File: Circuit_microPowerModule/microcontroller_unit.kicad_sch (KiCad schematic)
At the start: 1 part, among them U6 RP2040

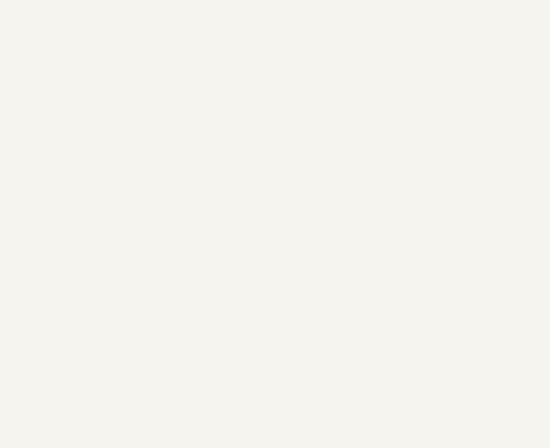
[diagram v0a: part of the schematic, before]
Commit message: added MP2315S lib, updated circuit
updated block diagram by-sa
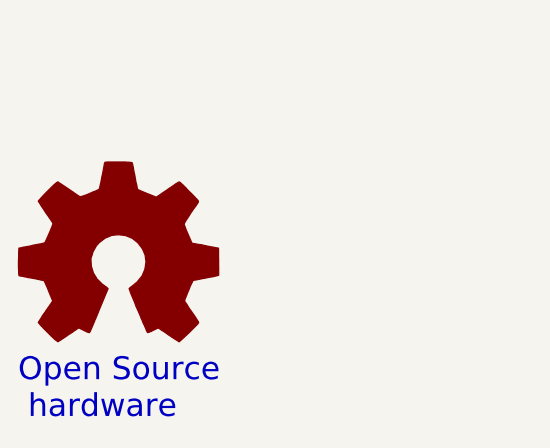
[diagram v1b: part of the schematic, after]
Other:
- note added: "Open Source hardware"

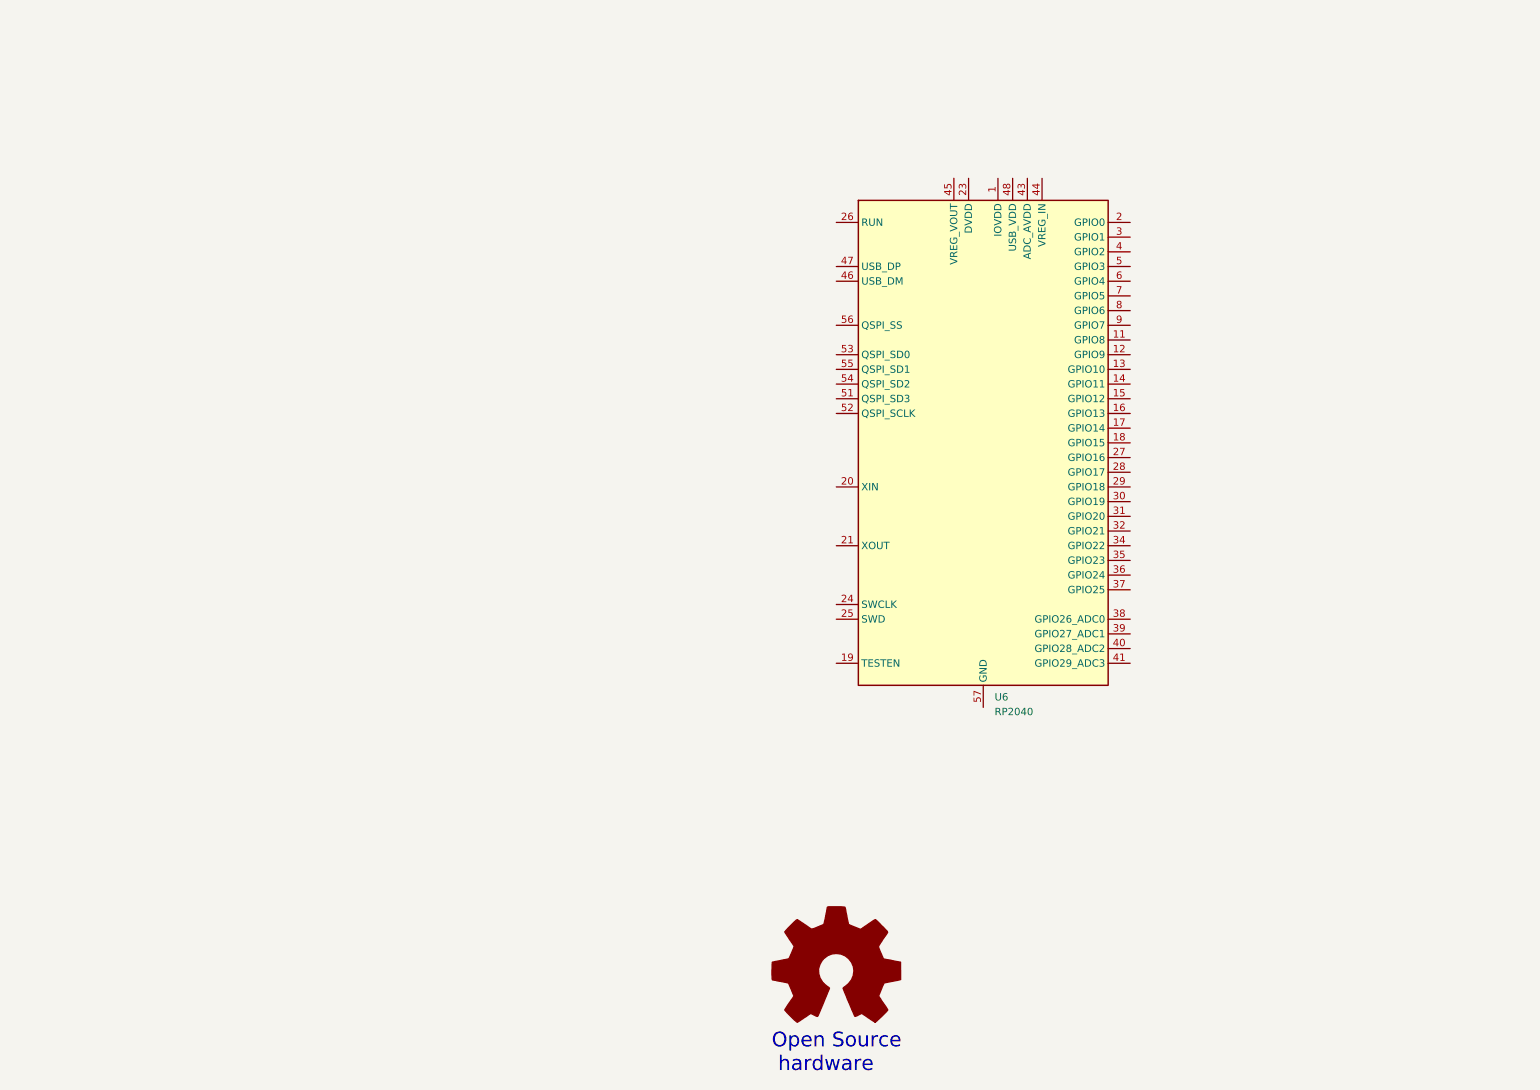
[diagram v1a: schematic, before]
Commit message: new RFQ, update circuit
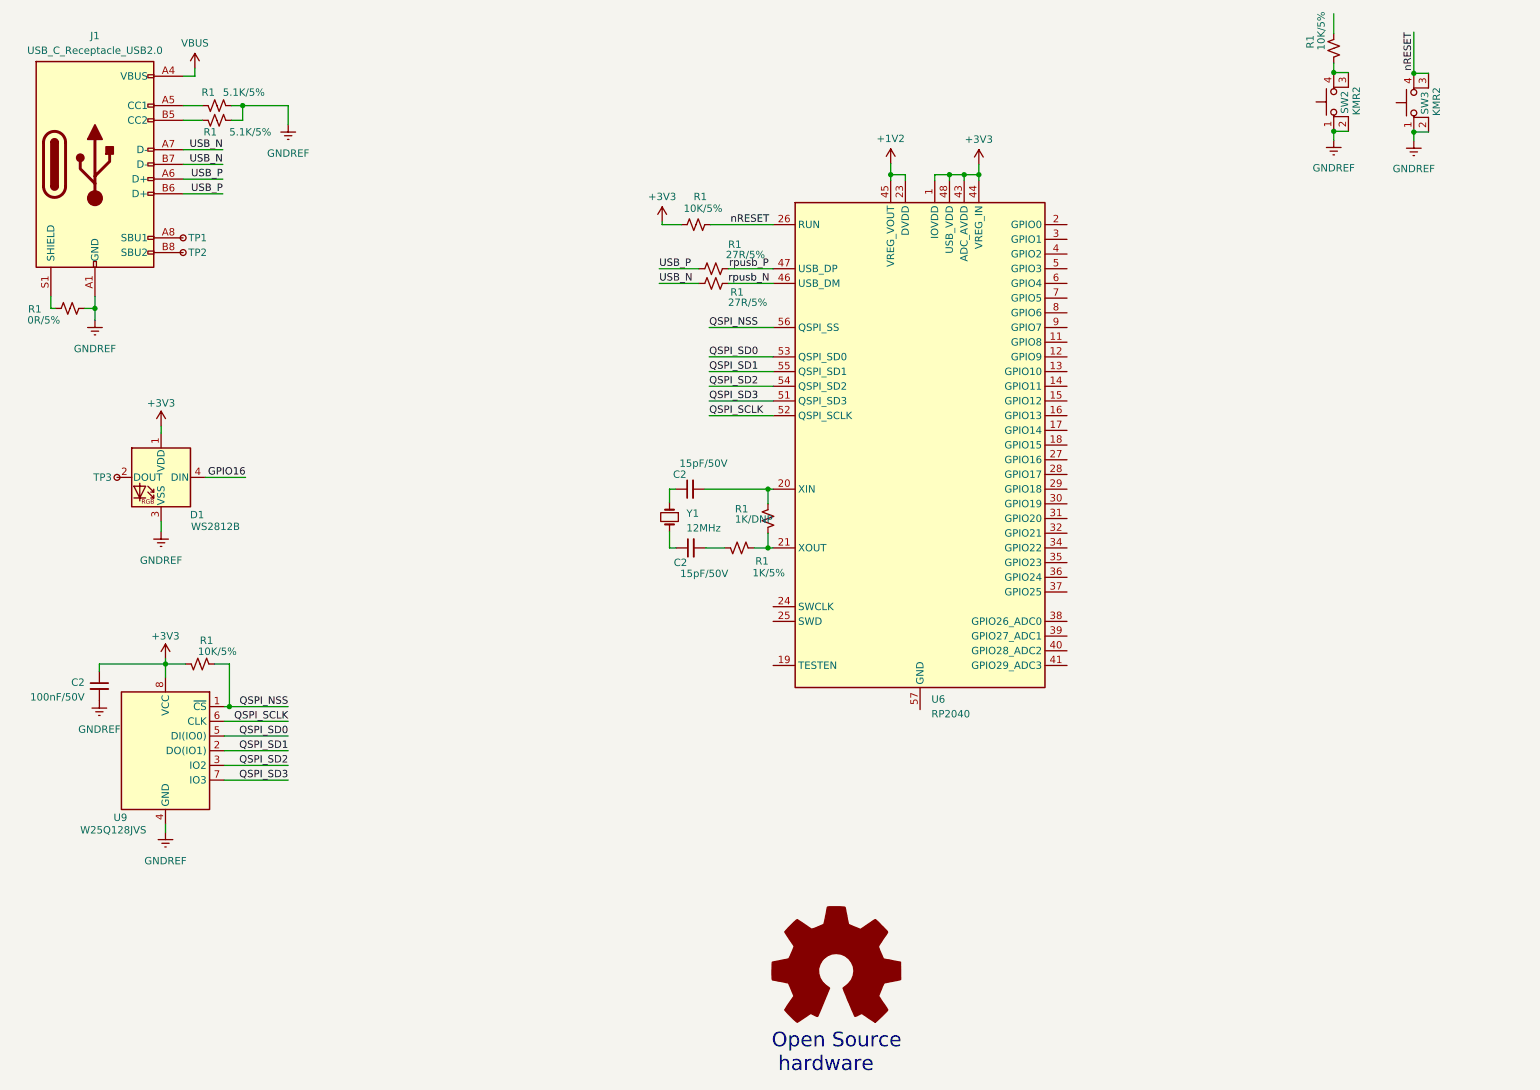
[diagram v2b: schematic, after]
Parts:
- added C2 (x2): 15pF/50V, symbol Device:C_Small
- added C2: 100nF/50V, symbol Device:C_Small
- added D1: WS2812B, LED_SMD:LED_WS2812B_PLCC4_5.0x5.0mm_P3.2mm, symbol LED:WS2812B
- added J1: USB_C_Receptacle_USB2.0, symbol Connector:USB_C_Receptacle_USB2.0
- added R1 (x2): 27R/5%, Resistor_SMD:R_0603_1608Metric, symbol Device:R_Small_US
- added R1 (x3): 10K/5%, Resistor_SMD:R_0603_1608Metric, symbol Device:R_Small_US
- added R1 (x2): 5.1K/5%, Resistor_SMD:R_0603_1608Metric, symbol Device:R_Small_US
- added R1: 1K/DNP, Resistor_SMD:R_0603_1608Metric, symbol Device:R_Small_US
- added R1: 1K/5%, Resistor_SMD:R_0603_1608Metric, symbol Device:R_Small_US
- added R1: 0R/5%, Resistor_SMD:R_0603_1608Metric, symbol Device:R_Small_US
- added SW2, SW3: KMR2, symbol Switch:SW_MEC_5E
- added TP1, TP2, TP3: TestPoint_Small, symbol Connector:TestPoint_Small
- added U9: W25Q128JVS, Package_SO:SOIC-8_5.23x5.23mm_P1.27mm, symbol Memory_Flash:W25Q128JVS
- added Y1: 12MHz, symbol Device:Crystal_Small
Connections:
- net +3V3: now reaches U6.1 (IOVDD), U6.10 (IOVDD), U6.22 (IOVDD), U6.33 (IOVDD), U6.42 (IOVDD), U6.49 (IOVDD)
- net +3V3: now also U6.43 (ADC_AVDD), U6.44 (VREG_IN), U6.48 (USB_VDD), C2.1, D1.1 (VDD), R1.2, R1.2, U9.8 (VCC)
- net at U6.20 (XIN): now also C2.2, R1.1
- net at U6.21 (XOUT): now also R1.1, R1.2
- net +1V2: now reaches U6.23 (DVDD), U6.50 (DVDD)
- net +1V2: now also U6.45 (VREG_VOUT)
- net nRESET: now reaches U6.26 (RUN)
- net nRESET: now also R1.1, SW3.3 (K), SW3.4 (A)
- net rpusb_N: now reaches U6.46 (USB_DM)
- net rpusb_N: now also R1.1
- net rpusb_P: now reaches U6.47 (USB_DP)
- net rpusb_P: now also R1.1
- net QSPI_SD3: now reaches U6.51 (QSPI_SD3)
- net QSPI_SD3: now also U9.7 (IO3)
- net QSPI_SCLK: now reaches U6.52 (QSPI_SCLK)
- net QSPI_SCLK: now also U9.6 (CLK)
- net QSPI_SD0: now reaches U6.53 (QSPI_SD0)
- net QSPI_SD0: now also U9.5 (DI(IO0))
- net QSPI_SD2: now reaches U6.54 (QSPI_SD2)
- net QSPI_SD2: now also U9.3 (IO2)
- net QSPI_SD1: now reaches U6.55 (QSPI_SD1)
- net QSPI_SD1: now also U9.2 (DO(IO1))
- net QSPI_NSS: now reaches U6.56 (QSPI_SS)
- net QSPI_NSS: now also R1.1, U9.1 (~{CS})
- new net: C2.1, Y1.1
- new net: C2.1, Y1.2
- new net: J1.B8 (SBU2), TP2.1
- new net: J1.B5 (CC2), R1.2
- new net: D1.2 (DOUT), TP3.1
- new net: J1.A5 (CC1), R1.1
- new net: C2.2, R1.2
- new net: J1.S1 (SHIELD), R1.1
- new net: J1.A8 (SBU1), TP1.1
- new net: R1.2, SW2.3 (K), SW2.4 (A)
- new net GNDREF: C2.2, D1.3 (VSS), J1.A1 (GND), J1.A12 (GND), J1.B1 (GND), J1.B12 (GND), R1.1, R1.2, R1.2, SW2.1, SW2.2, SW3.1, SW3.2, U9.4 (GND)
- new net GPIO16: D1.4 (DIN)
- new net USB_N: J1.A7 (D-), J1.B7 (D-), R1.2
- new net USB_P: J1.A6 (D+), J1.B6 (D+), R1.2
- new net VBUS: J1.A4 (VBUS), J1.A9 (VBUS), J1.B4 (VBUS), J1.B9 (VBUS)
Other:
- moved on the sheet: U6

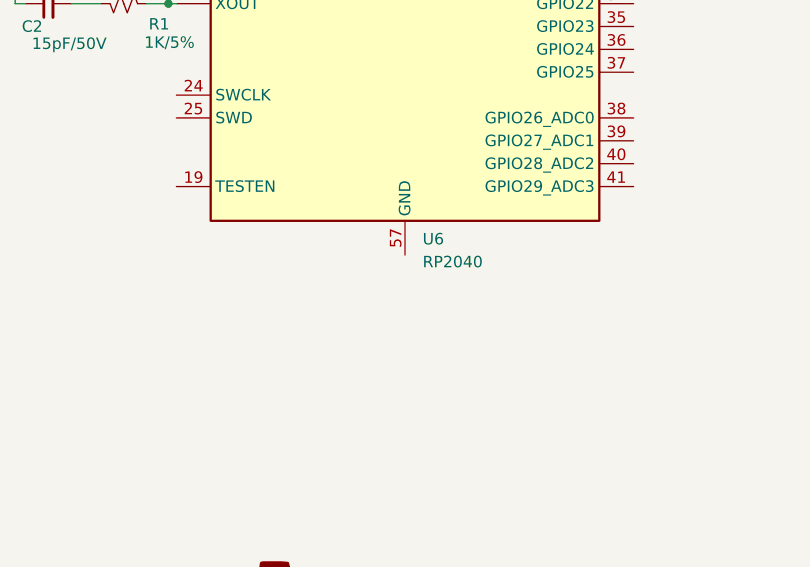
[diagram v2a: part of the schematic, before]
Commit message: added input power OVP circuit
update buck-boost circuit
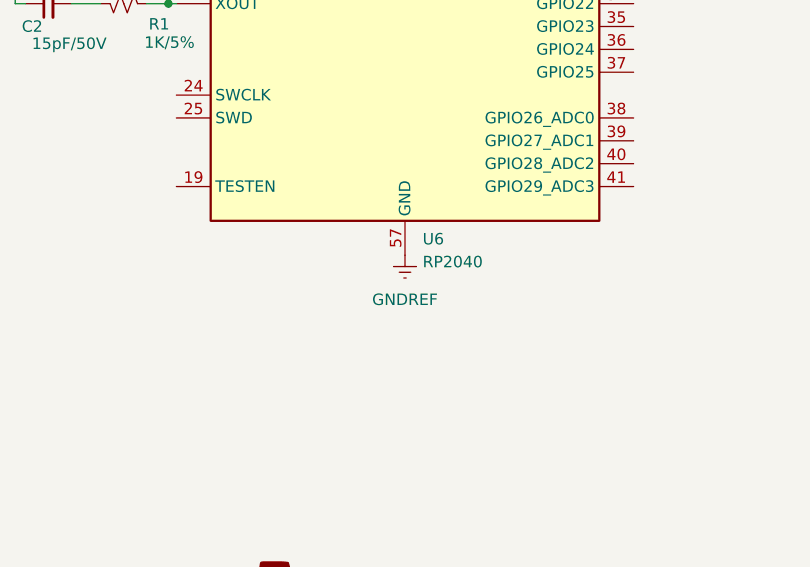
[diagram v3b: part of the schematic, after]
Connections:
- net GNDREF: now also U6.57 (GND)
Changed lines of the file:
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@@
+    )
+  )
+  (symbol (lib_id "power:GNDREF") (at 174.244 134.239 0) (unit 1)
+    (in_bom yes) (on_board yes) (dnp no) (fields_autoplaced)
+    (property "Reference" "#PWR024" (at 174.244 140.589 0)
+      (effects (font (size 1.27 1.27)) hide)
+    )
+    (property "Value" "GNDREF" (at 174.244 139.192 0)
+      (effects (font (size 1.27 1.27)))
+    )
+    (property "Footprint" "" (at 174.244 134.239 0)
+      (effects (font (size 1.27 1.27)) hide)
+    )
+    (property "Datasheet" "" (at 174.244 134.239 0)
+      (effects (font (size 1.27 1.27)) hide)
+    )
+    (pin "1")
+    (instances
+      (project "micro-PowerModule"
+        (path "/38b19d1a-a8d3-49c0-a6a2-bee4e845832f/7187d72d-86a6-4df3-a706-10f93237b261"
+          (reference "#PWR024") (unit 1)
+        )
+      )
     )
   )

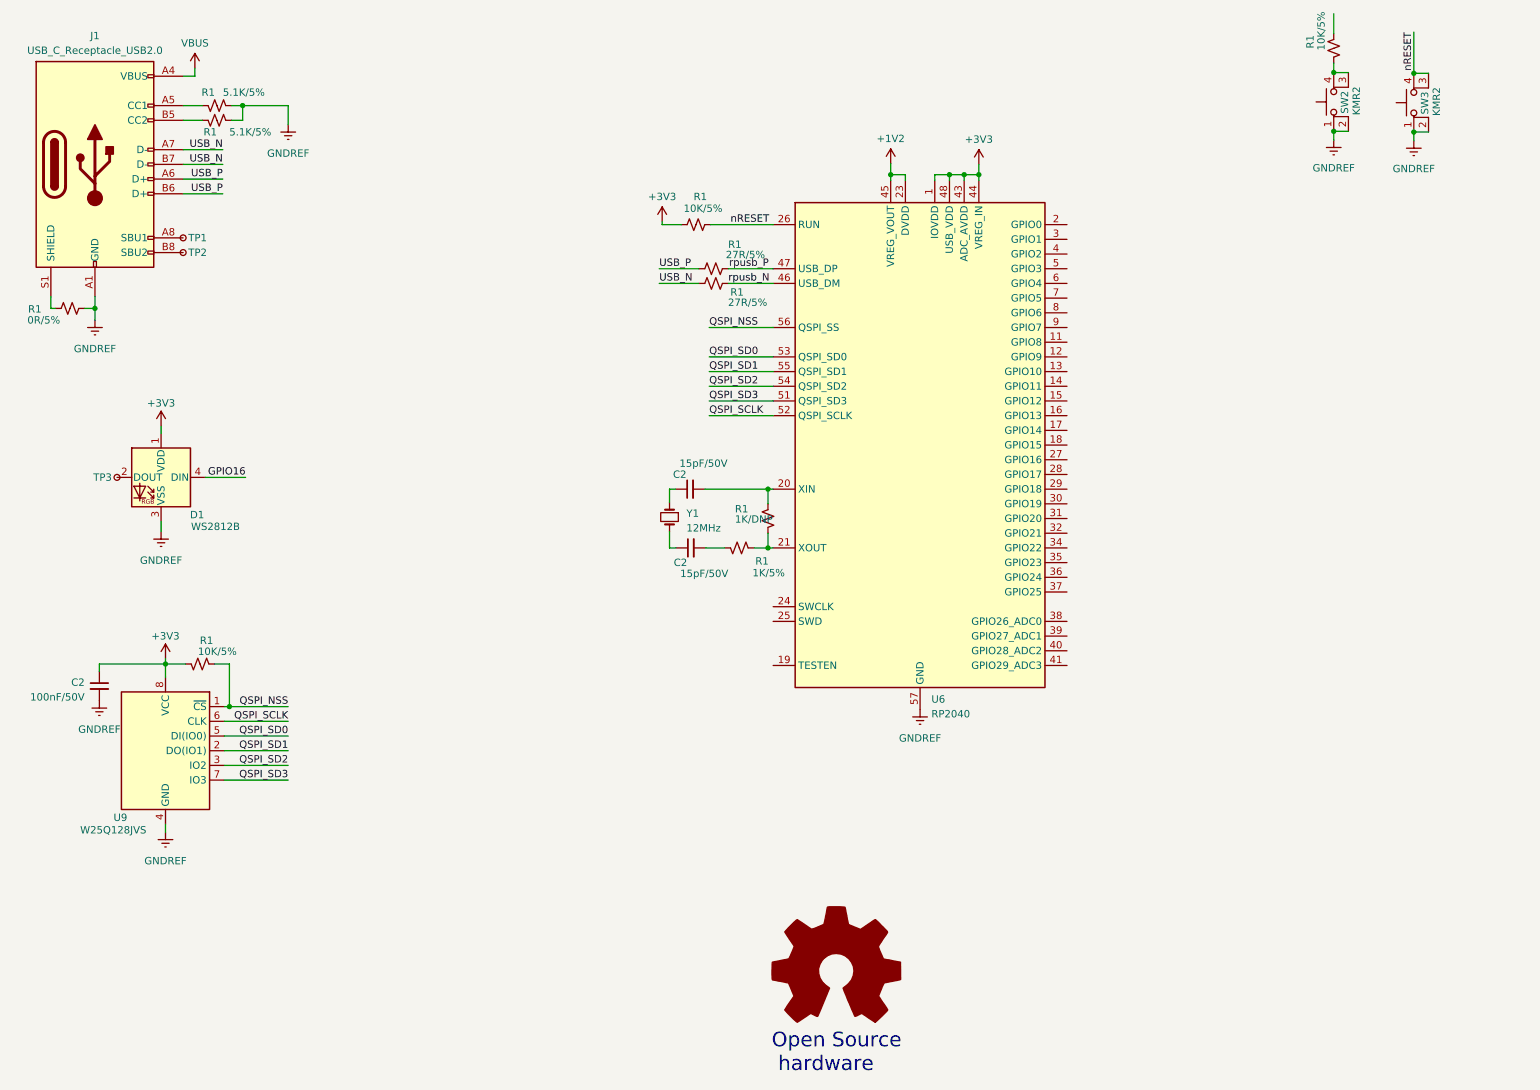
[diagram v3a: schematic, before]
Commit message: added boost circuit
create peripheral schematic
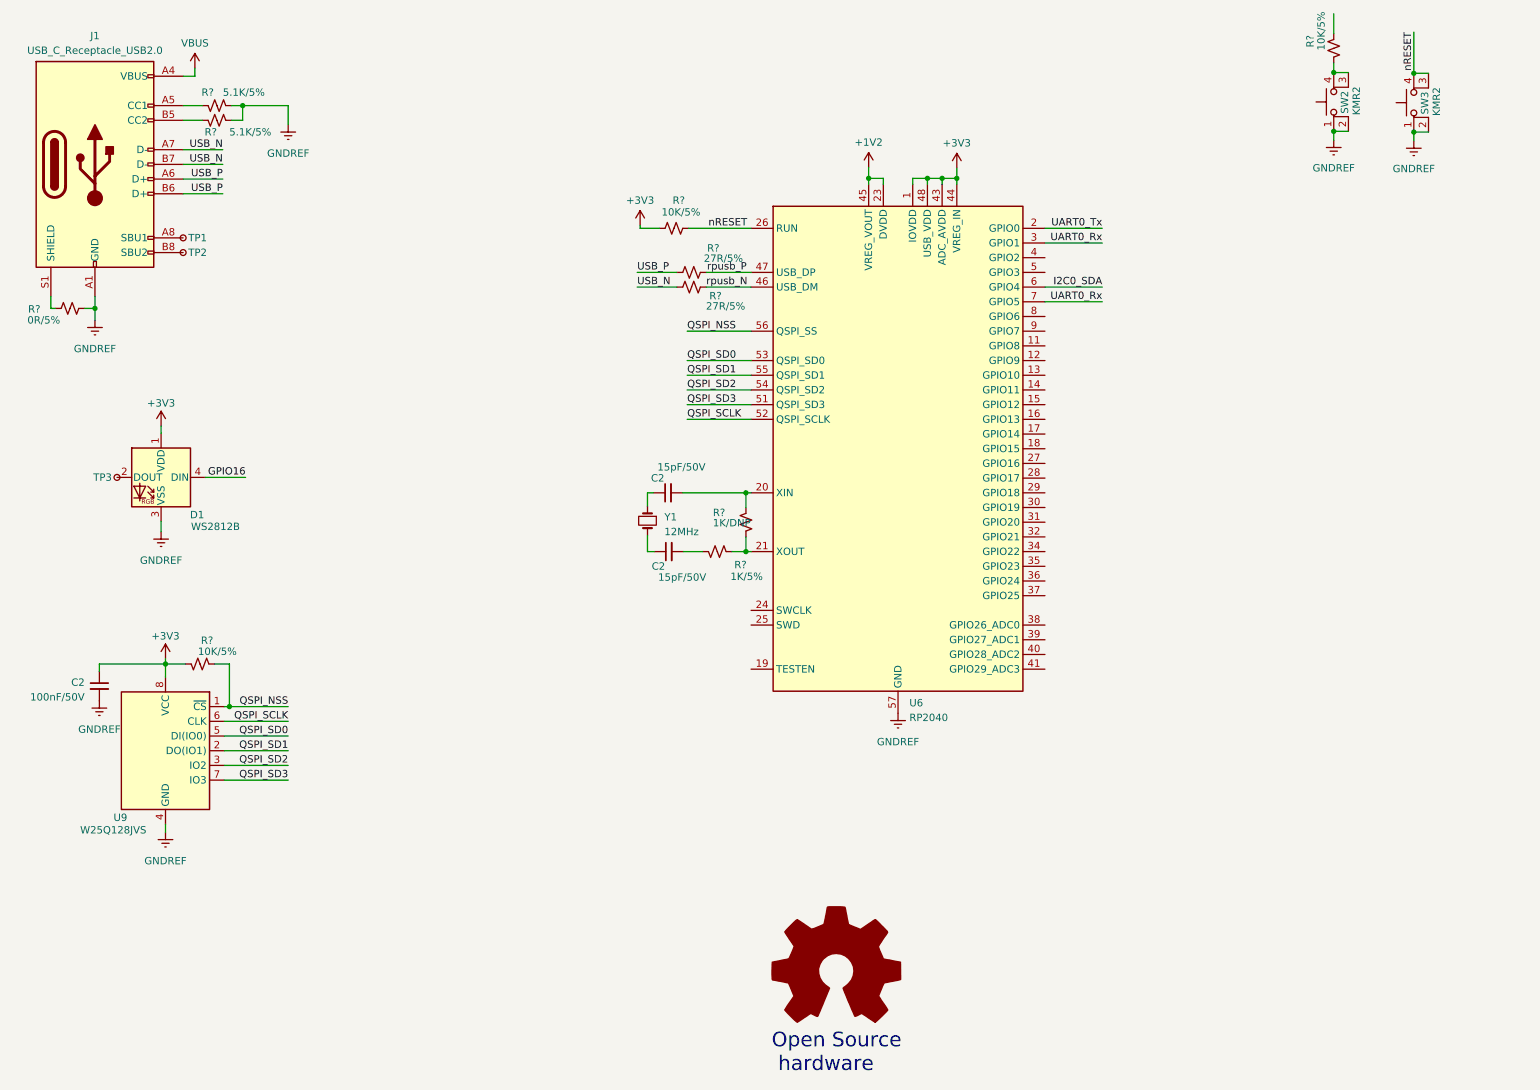
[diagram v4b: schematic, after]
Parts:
- renumbered R1 to R?
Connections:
- net UART0_Tx: now reaches U6.2 (GPIO0)
- net UART0_Rx: now reaches U6.3 (GPIO1)
- net UART0_Rx: now also U6.7 (GPIO5)
- net I2C0_SDA: now reaches U6.6 (GPIO4)
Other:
- moved on the sheet: C2, R?, U6, Y1
